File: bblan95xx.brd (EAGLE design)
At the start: 50 x 50 mm, 51 parts, among them IC1 LAN9512, IC2 93ST, Q1 25MHz

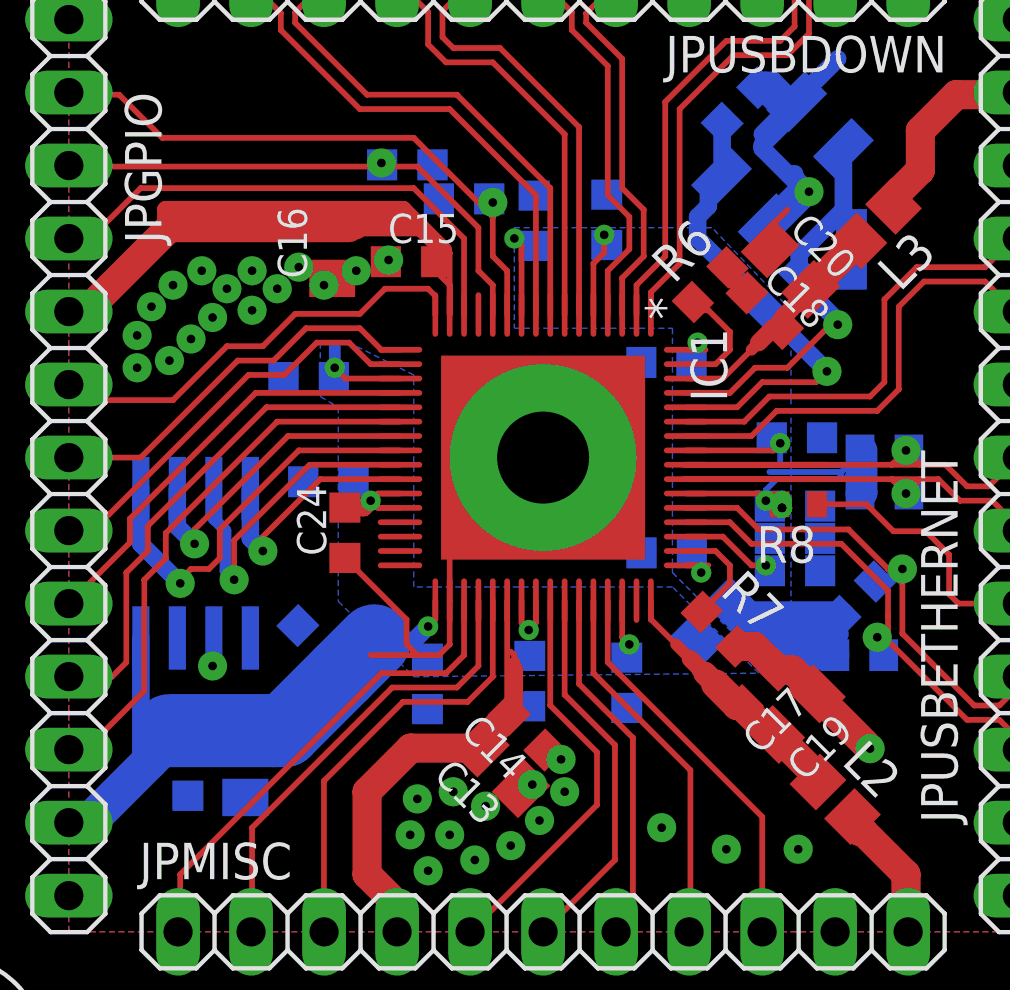
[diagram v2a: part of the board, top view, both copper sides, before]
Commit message: add extra 0603 cap and make 0603 to 0805 where possible
Signed-off-by: Stephan Baerwolf <stephan@matrixstorm.com>
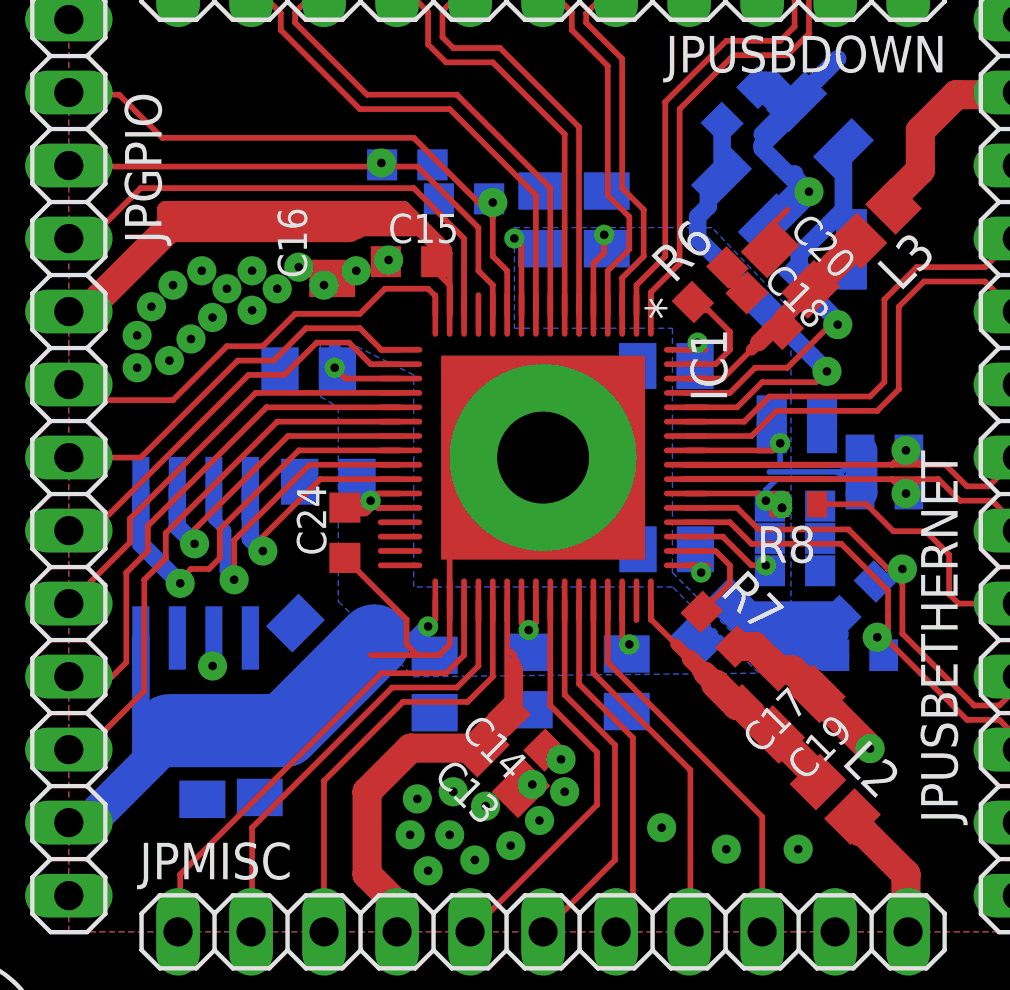
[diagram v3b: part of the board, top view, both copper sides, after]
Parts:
- added C30: .1u, resistor:C0603K
- C1, C12, C2, C26, C27, C3, C4, C5, C6, C7, C8: device resistor:C0603K -> resistor:C0805K
- moved C25 0.50 mm to (15.1, 14.2)
- moved C26 0.50 mm to (13.1, 14.1)
- moved C7 0.25 mm to (24.9, 33.3)
- moved C1 0.25 mm to (16.8, 28.0)
- moved C3 0.25 mm to (21.2, 17.1)
- moved C12 0.12 mm to (29.3, 28.2)
- moved C8 0.12 mm to (29.3, 21.8)
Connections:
- net GND: now also C30.1
- net VDD33A: now also C30.2
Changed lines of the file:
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@@
 </autorouter>
 <elements>
-<element name="C1" library="resistor" package="C0603K" value=".1u" x="16.845" y="27.785" smashed="yes" rot="MR180">
-<attribute name="SPICEPREFIX" value="C" x="16.845" y="27.785" size="1.778" layer="28" rot="MR180" display="off"/>
-<attribute name="NAME" x="16.045" y="27.135" size="1.016" layer="26" rot="MR180"/>
+<element name="C1" library="resistor" package="C0805K" value=".1u" x="16.845" y="28.035" smashed="yes" rot="MR180">
+<attribute name="SPICEPREFIX" value="C" x="16.845" y="28.035" size="1.778" layer="28" rot="MR180" display="off"/>
+<attribute name="NAME" x="16.045" y="27.385" size="1.016" layer="26" rot="MR180"/>
 </element>
 <element name="C10" library="resistor" package="C0603K" value=".1u" x="33.765" y="23.315" smashed="yes" rot="MR0">
@@
 <attribute name="NAME" x="34.63" y="26.34" size="1.016" layer="26" rot="MR0"/>
 </element>
-<element name="C12" library="resistor" package="C0603K" value=".1u" x="29.29" y="28.31" smashed="yes" rot="MR180">
-<attribute name="SPICEPREFIX" value="C" x="29.29" y="28.31" size="1.778" layer="28" rot="MR180" display="off"/>
-<attribute name="NAME" x="28.49" y="27.66" size="1.016" layer="26" rot="MR180"/>
+<element name="C12" library="resistor" package="C0805K" value=".1u" x="29.29" y="28.185" smashed="yes" rot="MR180">
+<attribute name="SPICEPREFIX" value="C" x="29.29" y="28.185" size="1.778" layer="28" rot="MR180" display="off"/>
+<attribute name="NAME" x="28.49" y="27.535" size="1.016" layer="26" rot="MR180"/>
 </element>
 <element name="C13" library="resistor" package="C0805K" value="4.7u" x="23.52475" y="14.185103125" rot="R135">
@@
 <attribute name="SPICEPREFIX" value="C" x="35.726615625" y="32.2466125" size="1.778" layer="28" rot="MR90" display="off"/>
 </element>
-<element name="C2" library="resistor" package="C0603K" value=".1u" x="17.53" y="24.16" smashed="yes" rot="MR180">
+<element name="C2" library="resistor" package="C0805K" value=".1u" x="17.53" y="24.16" smashed="yes" rot="MR180">
 <attribute name="SPICEPREFIX" value="C" x="17.53" y="24.16" size="1.778" layer="28" rot="MR180" display="off"/>
 <attribute name="NAME" x="16.73" y="23.51" size="1.016" layer="26" rot="MR180"/>
@@
 <attribute name="NAME" x="17.455" y="21.585" size="1.016" layer="25" rot="R90"/>
 </element>
-<element name="C25" library="resistor" package="C0805K" value="1u" x="14.645" y="14.175" smashed="yes" rot="MR90">
-<attribute name="SPICEPREFIX" value="C" x="14.645" y="14.175" size="1.778" layer="28" rot="MR90" display="off"/>
-<attribute name="NAME" x="15.52" y="13.175" size="1.016" layer="26" rot="MR90"/>
-</element>
-<element name="C26" library="resistor" package="C0603K" value=".1u" x="12.645" y="14.11" smashed="yes" rot="MR90">
-<attribute name="SPICEPREFIX" value="C" x="12.645" y="14.11" size="1.778" layer="28" rot="MR90" display="off"/>
-<attribute name="NAME" x="13.295" y="13.31" size="1.016" layer="26" rot="MR90"/>
-</element>
-<element name="C3" library="resistor" package="C0603K" value=".1u" x="20.976271875" y="17.124996875" smashed="yes" rot="MR90">
-<attribute name="SPICEPREFIX" value="C" x="20.976271875" y="17.124996875" size="1.778" layer="28" rot="MR90" display="off"/>
-<attribute name="NAME" x="21.62626875" y="16.324996875" size="1.016" layer="26" rot="MR90"/>
-</element>
-<element name="C4" library="resistor" package="C0603K" value=".1u" x="24.535" y="17.225" smashed="yes" rot="MR90">
+<element name="C25" library="resistor" package="C0805K" value="1u" x="15.145" y="14.175" smashed="yes" rot="MR90">
+<attribute name="SPICEPREFIX" value="C" x="15.145" y="14.175" size="1.778" layer="28" rot="MR90" display="off"/>
+<attribute name="NAME" x="16.02" y="13.175" size="1.016" layer="26" rot="MR90"/>
+</element>
+<element name="C26" library="resistor" package="C0805K" value=".1u" x="13.145" y="14.11" smashed="yes" rot="MR90">
+<attribute name="SPICEPREFIX" value="C" x="13.145" y="14.11" size="1.778" layer="28" rot="MR90" display="off"/>
+<attribute name="NAME" x="13.795" y="13.31" size="1.016" layer="26" rot="MR90"/>
+</element>
+<element name="C3" library="resistor" package="C0805K" value=".1u" x="21.226271875" y="17.124996875" smashed="yes" rot="MR90">
+<attribute name="SPICEPREFIX" value="C" x="21.226271875" y="17.124996875" size="1.778" layer="28" rot="MR90" display="off"/>
+<attribute name="NAME" x="21.87626875" y="16.324996875" size="1.016" layer="26" rot="MR90"/>
+</element>
+<element name="C4" library="resistor" package="C0805K" value=".1u" x="24.535" y="17.225" smashed="yes" rot="MR90">
 <attribute name="SPICEPREFIX" value="C" x="24.535" y="17.225" size="1.778" layer="28" rot="MR90" display="off"/>
 <attribute name="NAME" x="25.185" y="16.425" size="1.016" layer="26" rot="MR90"/>
 </element>
-<element name="C5" library="resistor" package="C0603K" value=".1u" x="27.91" y="17.165" smashed="yes" rot="MR90">
+<element name="C5" library="resistor" package="C0805K" value=".1u" x="27.91" y="17.165" smashed="yes" rot="MR90">
 <attribute name="SPICEPREFIX" value="C" x="27.91" y="17.165" size="1.778" layer="28" rot="MR90" display="off"/>
 <attribute name="NAME" x="28.56" y="16.365" size="1.016" layer="26" rot="MR90"/>
 </element>
-<element name="C6" library="resistor" package="C0603K" value=".1u" x="27.215" y="33.27" smashed="yes" rot="MR270">
+<element name="C6" library="resistor" package="C0805K" value=".1u" x="27.215" y="33.27" smashed="yes" rot="MR270">
 <attribute name="SPICEPREFIX" value="C" x="27.215" y="33.27" size="1.778" layer="28" rot="MR270" display="off"/>
 <attribute name="NAME" x="26.565" y="34.07" size="1.016" layer="26" rot="MR270"/>
 </element>
-<element name="C7" library="resistor" package="C0603K" value=".1u" x="24.69" y="33.24" smashed="yes" rot="MR270">
-<attribute name="SPICEPREFIX" value="C" x="24.69" y="33.24" size="1.778" layer="28" rot="MR270" display="off"/>
-<attribute name="NAME" x="24.04" y="34.04" size="1.016" layer="26" rot="MR270"/>
-</element>
-<element name="C8" library="resistor" package="C0603K" value=".1u" x="29.3" y="21.685" smashed="yes" rot="MR180">
-<attribute name="SPICEPREFIX" value="C" x="29.3" y="21.685" size="1.778" layer="28" rot="MR180" display="off"/>
-<attribute name="NAME" x="28.5" y="21.035" size="1.016" layer="26" rot="MR180"/>
+<element name="C7" library="resistor" package="C0805K" value=".1u" x="24.94" y="33.27" smashed="yes" rot="MR270">
+<attribute name="SPICEPREFIX" value="C" x="24.94" y="33.27" size="1.778" layer="28" rot="MR270" display="off"/>
+<attribute name="NAME" x="24.29" y="34.07" size="1.016" layer="26" rot="MR270"/>
+</element>
+<element name="C8" library="resistor" package="C0805K" value=".1u" x="29.3" y="21.81" smashed="yes" rot="MR180">
+<attribute name="SPICEPREFIX" value="C" x="29.3" y="21.81" size="1.778" layer="28" rot="MR180" display="off"/>
+<attribute name="NAME" x="28.5" y="21.16" size="1.016" layer="26" rot="MR180"/>
 </element>
 <element name="C9" library="resistor" package="C0603K" value=".1u" x="33.765" y="21.065" smashed="yes" rot="MR0">
@@
 <attribute name="SPICEPREFIX" value="C" x="33.801775" y="16.073221875" size="1.778" layer="27" rot="R225" display="off"/>
 </element>
-<element name="C27" library="resistor" package="C0603K" value=".1u" x="17.0883875" y="18.536609375" smashed="yes" rot="MR225">
+<element name="C27" library="resistor" package="C0805K" value=".1u" x="17.0883875" y="18.536609375" smashed="yes" rot="MR225">
 <attribute name="SPICEPREFIX" value="C" x="17.0883875" y="18.536609375" size="1.778" layer="28" rot="MR225" display="off"/>
 <attribute name="NAME" x="16.06308125" y="18.642675" size="1.016" layer="26" rot="MR225"/>
@@
 <element name="R8" library="resistor" package="R0402" value="" x="33.875" y="23.375" rot="R180">
 <attribute name="SPICEPREFIX" value="R" x="33.875" y="23.375" size="1.778" layer="27" rot="R180" display="off"/>
+</element>
+<element name="C30" library="resistor" package="C0603K" value=".1u" x="33.83" y="26.625" rot="MR0">
+<attribute name="SPICEPREFIX" value="C" x="33.83" y="26.625" size="1.778" layer="28" rot="MR0" display="off"/>
 </element>
 </elements>
@@
 <wire x1="11.005" y1="18.725" x2="11.005" y2="14.745" width="0.6096" layer="16"/>
 <wire x1="11.005" y1="14.745" x2="11.3125" y2="14.4375" width="0.6096" layer="16"/>
-<wire x1="12.645" y1="14.985" x2="12.39" y2="14.985" width="0.2" layer="16"/>
+<wire x1="13.145" y1="15.11" x2="12.39" y2="14.985" width="0.2" layer="16"/>
 <wire x1="12.39" y1="14.985" x2="12" y2="15.375" width="0.2" layer="16"/>
-<wire x1="14.645" y1="15.175" x2="15.3" y2="15.175" width="0.2" layer="16"/>
+<wire x1="15.145" y1="15.175" x2="15.3" y2="15.175" width="0.2" layer="16"/>
 <wire x1="15.3" y1="15.175" x2="15.625" y2="15.5" width="0.2" layer="16"/>
 <contactref element="C27" pad="2"/>
-<wire x1="17.70710625" y1="17.917890625" x2="18" y2="17.624996875" width="0.6096" layer="16"/>
+<wire x1="17.795496875" y1="17.8295" x2="18" y2="17.624996875" width="0.6096" layer="16"/>
 <wire x1="18" y1="17.624996875" x2="18" y2="17.5" width="0.6096" layer="16"/>
-<wire x1="17.75" y1="27.815" x2="17.72" y2="27.785" width="0.6096" layer="16"/>
+<wire x1="17.75" y1="27.815" x2="17.845" y2="28.035" width="0.6096" layer="16"/>
 <wire x1="17.75" y1="28.875" x2="17.75" y2="28.125" width="0.4064" layer="16"/>
 </signal>
@@
 <wire x1="33.225" y1="23.375" x2="33.3125" y2="23.375" width="0.2" layer="1"/>
 <wire x1="33.3125" y1="23.375" x2="33.3125" y2="23.5" width="0.2" layer="1"/>
+<contactref element="C30" pad="2"/>
 </signal>
 <signal name="GND">
@@
 <wire x1="32.625" y1="36.25" x2="33.375" y2="37" width="0.6096" layer="16"/>
 <contactref element="C29" pad="1"/>
+<contactref element="C30" pad="1"/>
 </signal>
 <signal name="VDD18CORE">
